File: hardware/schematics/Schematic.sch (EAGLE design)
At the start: 28 parts, among them IC1 MEGA8-AI, IC2 MC33269D-3.3, U1 MCP73831, U2 TPS61200, X1 USB-MICROB, Y1 16 mhz

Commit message: more updated schematic
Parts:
- added D1, D2: 1N4004, diode:1N4004
- added Q1, Q2, Q3, Q4: 2N5087, transistor-pnp:2N5087
- added R10, R14, R15, R8: 10k, SparkFun:RESISTOR0402-RES
- added R11, R12, R13, R2, R3, R4: 1k, SparkFun:RESISTOR0402-RES
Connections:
- new net N$12: D1.C, R4.1
- new net N$4: Q1.C, R10.2, R2.1
- new net N$5: Q3.C, R11.1, R15.2
- new net N$6: D2.A, Q4.C, R12.1, R14.1
- new net N$7: D1.A, Q2.C, R3.1, R8.1
- new net N$9: D2.C, R13.1
- new net PIR_SENSOR: IC1.PD2(INT0)
- new net RELAY1: R4.2
- new net RELAY2: R13.2
- new net RELAYCTL1: IC1.PC0(ADC0), Q1.B, R8.2
- new net RELAYCTL2: IC1.PC1(ADC1), Q2.B, R10.1
- new net RELAYCTL3: IC1.PC2(ADC2), Q3.B, R14.2
- new net RELAYCTL4: IC1.PC3(ADC3), Q4.B, R15.1
- net GND: now also Q1.E, Q2.E, Q3.E, Q4.E
- net SUPPLY_5V: now also R11.2, R12.2, R2.2, R3.2
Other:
- note added: "Processor"
- note added: "Relay Controllers"
- moved on the sheet: BLUETOOTH_DTR, BLUETOOTH_SERIAL_PORT, C1, C10, C2, C3, C9, D4, IC1, JP1, JP12, JP9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

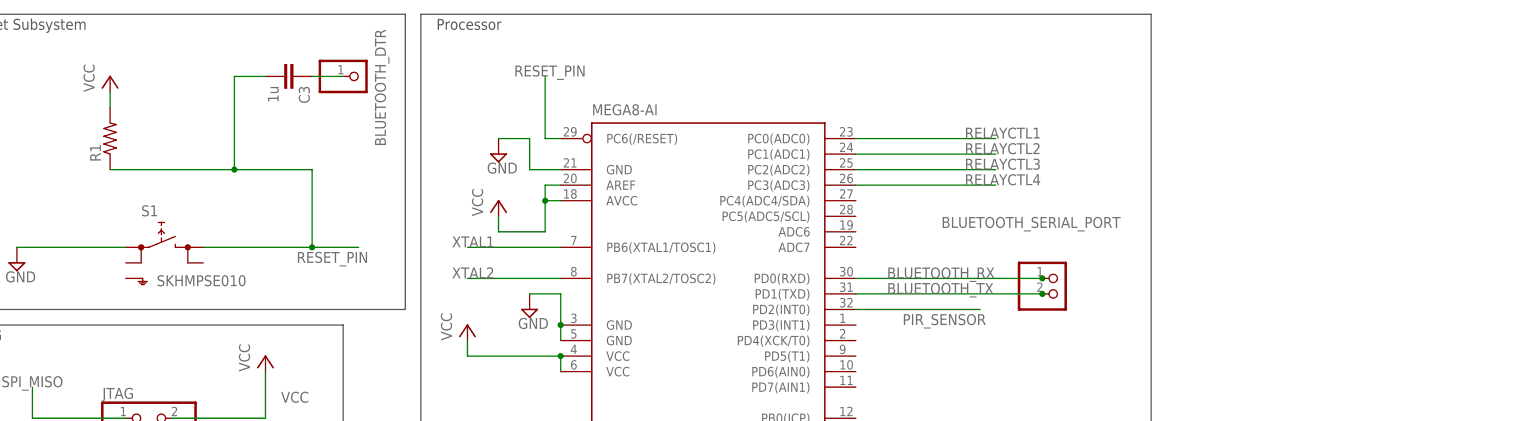
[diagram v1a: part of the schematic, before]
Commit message: better headers
fixed bluetooth header. still need to change PNP transistors to NMOS.
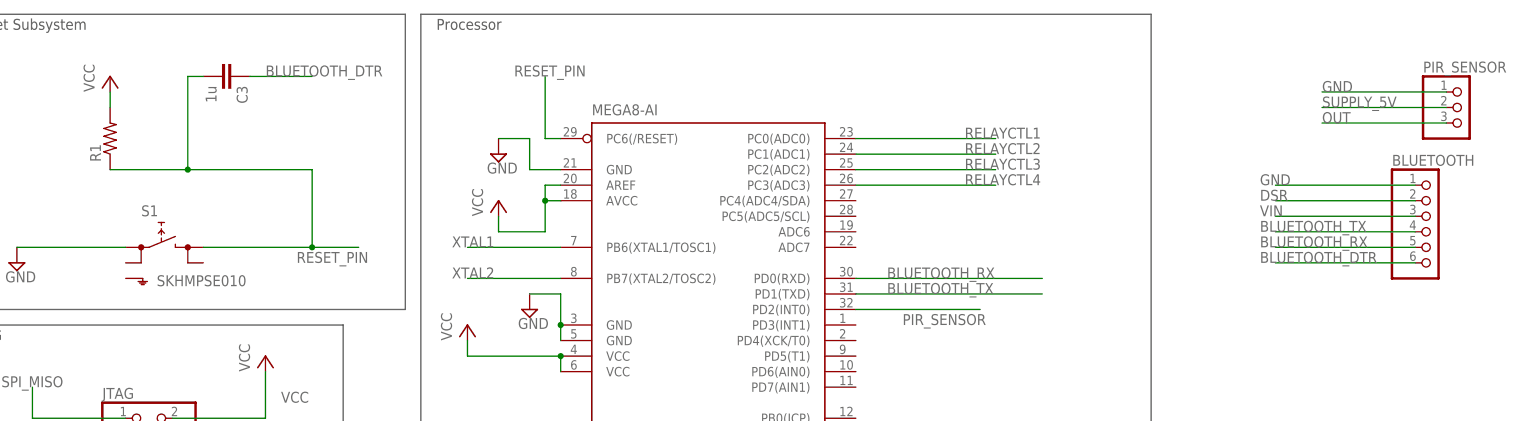
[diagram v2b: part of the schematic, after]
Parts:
- removed BLUETOOTH_DTR: (no value), pinhead:PINHD-1X1
- removed BLUETOOTH_SERIAL_PORT: (no value), pinhead:PINHD-1X2
- added BLUETOOTH: (no value), pinhead:PINHD-1X6
- added PIR_SENSOR: (no value), pinhead:PINHD-1X3
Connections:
- removed net N$1: BLUETOOTH_DTR.1, C3.1
- new net BLUETOOTH_DTR: BLUETOOTH.6, C3.1
- new net DSR: BLUETOOTH.2
- new net OUT: PIR_SENSOR.3
- new net VIN: BLUETOOTH.3
- net BLUETOOTH_RX: now also BLUETOOTH.5; no longer BLUETOOTH_SERIAL_PORT.1
- net BLUETOOTH_TX: now also BLUETOOTH.4; no longer BLUETOOTH_SERIAL_PORT.2
- net GND: now also BLUETOOTH.1, PIR_SENSOR.1
- net SUPPLY_5V: now also PIR_SENSOR.2
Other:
- moved on the sheet: C3
